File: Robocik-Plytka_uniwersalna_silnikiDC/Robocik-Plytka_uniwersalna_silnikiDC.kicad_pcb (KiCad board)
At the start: 2 copper layers, 60 x 66.8 mm, 67 parts, among them IC1 ACSL-6400-00TE, IC2 L6205D, J1 Conn_01x03, J2 Conn_01x02, J3 Conn_01x04, J4 Conn_01x02, J5 Conn_01x03, J6 Conn_01x02, Q1 BC847, Q2 BC847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

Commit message: Added connectors description on board.
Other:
- board text added: "CAN"
- board text added: "DC driver PCB v1"
- board text added: "Digital 5V"
- board text added: "Engines 16V"
- board text added: "Engines OUT"
- board text added: "UART"
- board text added: "programmer"
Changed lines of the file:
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@@
   (general
     (thickness 1.6)
-    (drawings 7)
+    (drawings 14)
     (tracks 496)
     (zones 0)
@@
     )
   )
+  (gr_text "DC driver PCB v1" (at 124.5 77.6 90) (layer F.SilkS)
+    (effects (font (size 1 1) (thickness 0.15)))
+  )
+  (gr_text "Engines OUT" (at 124 130.5 90) (layer F.SilkS)
+    (effects (font (size 1 1) (thickness 0.15)))
+  )
+  (gr_text "Engines 16V" (at 168.6 130.8 90) (layer F.SilkS)
+    (effects (font (size 1 1) (thickness 0.15)))
+  )
+  (gr_text UART (at 180.2 114.2 90) (layer F.SilkS)
+    (effects (font (size 1 1) (thickness 0.15)))
+  )
+  (gr_text CAN (at 180.2 103.3 90) (layer F.SilkS)
+    (effects (font (size 1 1) (thickness 0.15)))
+  )
+  (gr_text programmer (at 180 91.8 90) (layer F.SilkS)
+    (effects (font (size 1 1) (thickness 0.15)))
+  )
+  (gr_text "Digital 5V" (at 180.2 77.8 90) (layer F.SilkS)
+    (effects (font (size 1 1) (thickness 0.15)))
+  )
   (dimension 66.8 (width 0.15) (layer Dwgs.User)
     (gr_text "66,800 mm" (at 194.8 102.7 270) (layer Dwgs.User)
@@
   (gr_line (start 122.1 69.3) (end 122.1 135.5) (layer Edge.Cuts) (width 0.1))
   (gr_line (start 182.1 69.3) (end 122.1 69.3) (layer Edge.Cuts) (width 0.1))
-  (segment (start 143.93201 107.053222) (end 143.93201 109.16799) (width 0.25) (layer F.Cu) (net 76))
-  (segment (start 144 106.8) (end 144 106.985232) (width 0.25) (layer F.Cu) (net 76))
-  (segment (start 144 106.985232) (end 143.93201 107.053222) (width 0.25) (layer F.Cu) (net 76))
   (segment (start 145.176 95.051002) (end 145.866488 95.74149) (width 0.25) (layer F.Cu) (net 1))
   (segment (start 145.176 93.6045) (end 145.176 95.051002) (width 0.25) (layer F.Cu) (net 1))
@@
   (segment (start 141.609 81.568) (end 141.478 81.437) (width 0.5) (layer F.Cu) (net 75))
   (segment (start 143.942 81.568) (end 141.609 81.568) (width 0.5) (layer F.Cu) (net 75))
+  (segment (start 143.93201 107.053222) (end 143.93201 109.16799) (width 0.25) (layer F.Cu) (net 76))
+  (segment (start 144 106.8) (end 144 106.985232) (width 0.25) (layer F.Cu) (net 76))
+  (segment (start 144 106.985232) (end 143.93201 107.053222) (width 0.25) (layer F.Cu) (net 76))
   (via (at 143.256 116.84) (size 0.8) (drill 0.4) (layers F.Cu B.Cu) (net 76))
   (via (at 143.51 123.19) (size 0.8) (drill 0.4) (layers F.Cu B.Cu) (net 76))

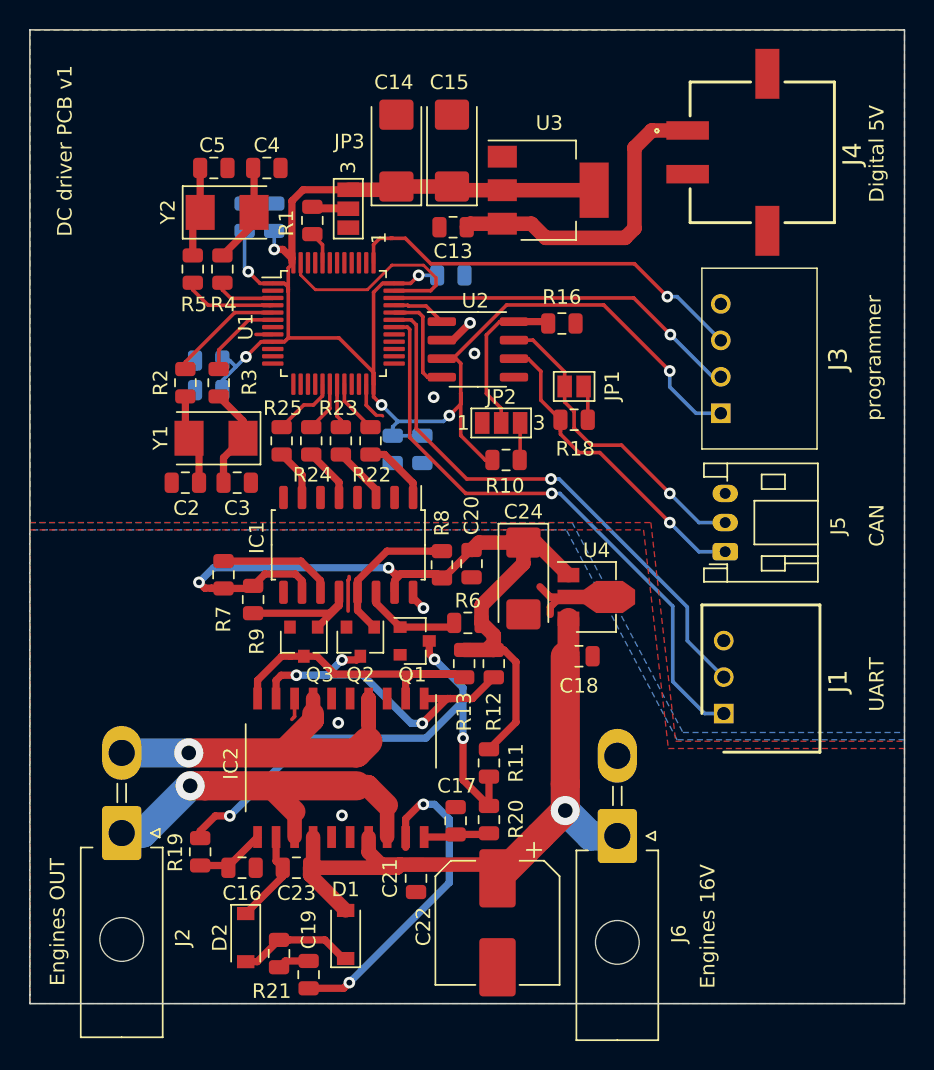
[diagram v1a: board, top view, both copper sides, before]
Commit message: Added missing 3D model for optocoupler. Moved all connector to the other side of the board. Reduced PCB size.
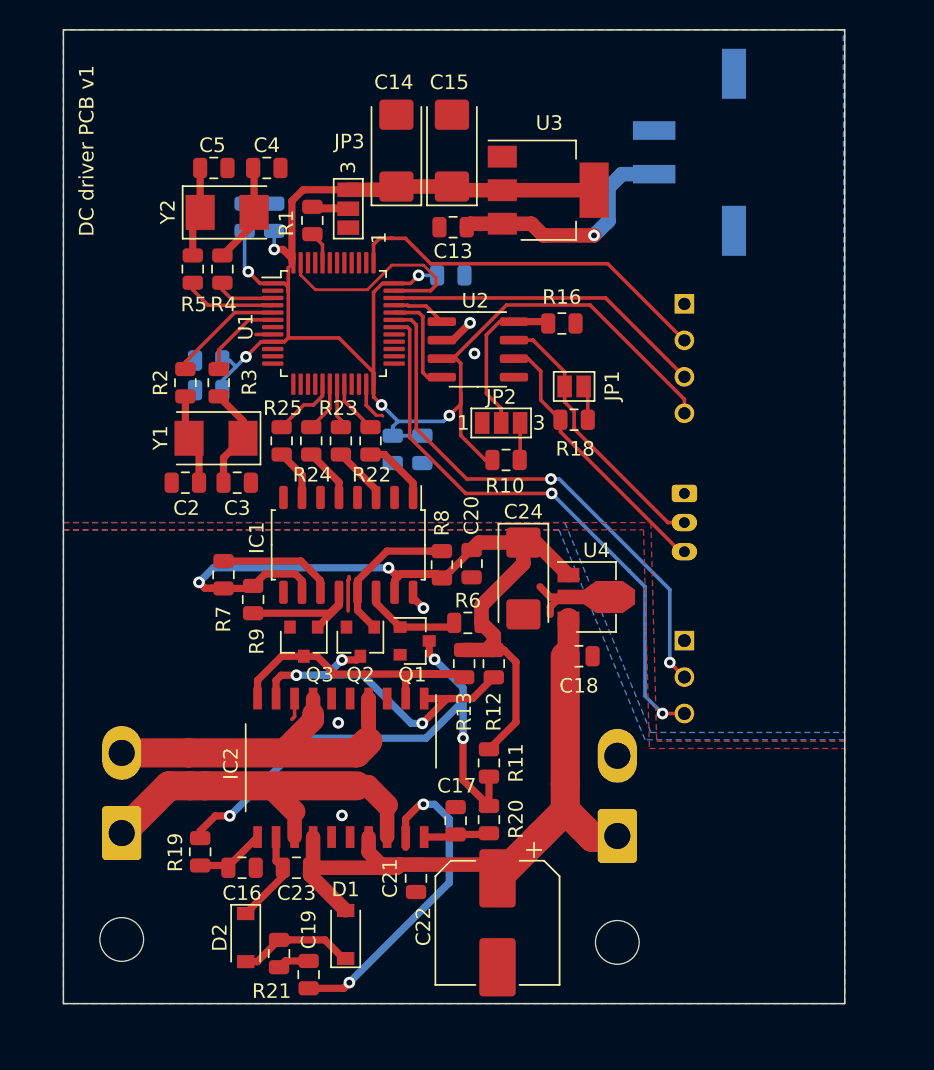
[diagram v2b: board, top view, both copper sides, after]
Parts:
- J1, J2, J3, J4, J5, J6: moved to B.Cu
- moved J3 7.91 mm to (167.0, 88.1), turned to 90 degrees
- moved J1 5.68 mm to (167.0, 111.2), turned to 90 degrees
- moved J5 4.88 mm to (167.0, 101.1), turned to 270 degrees
- moved J4 2.29 mm to (175.0, 77.7), turned to 270 degrees
- turned J2 to 0 degrees
- turned J6 to 0 degrees
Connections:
- J1 pad 1: USART_RX -> GNDD
- J1 pad 3: GNDD -> USART_RX
- J3 pad 1: 3.3VD -> GNDD
- J3 pad 2: JTMS_SWDIO -> JTCK_SWCLK
- J3 pad 3: JTCK_SWCLK -> JTMS_SWDIO
- J3 pad 4: GNDD -> 3.3VD
- J5 pad 1: CAN_L -> GNDD
- J5 pad 3: GNDD -> CAN_L
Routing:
- net VddD: track 21.9 -> 16.7 mm, vias 0 -> 1
- net CAN_L: track 22.9 -> 18.8 mm, vias 1 -> 0
- net JTMS_SWDIO: track 25.0 -> 22.2 mm, vias 1 -> 0
- net CAN_H: track 21.6 -> 18.8 mm, vias 1 -> 0
- net JTCK_SWCLK: track 28.5 -> 25.8 mm, vias 1 -> 0
- net 3.3VD: track 118.8 -> 116.2 mm, vias 7 -> 6
- net USART_RX: track 41.0 -> 39.6 mm, vias 1 -> 2
- net USART_TX: track 38.3 -> 37.2 mm, vias 1 -> 2
- net VddPWR: track 47.1 -> 47.3 mm, vias 1 -> 0
- net GNDD: vias 3 -> 2
- net ENG2: vias 1 -> 0
- net ENG1: vias 1 -> 0
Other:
- board size 60 x 66.8 mm -> 53.6 x 66.8 mm

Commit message: Further reduce of PCB size - moved description of every connector away from the border of PCB.
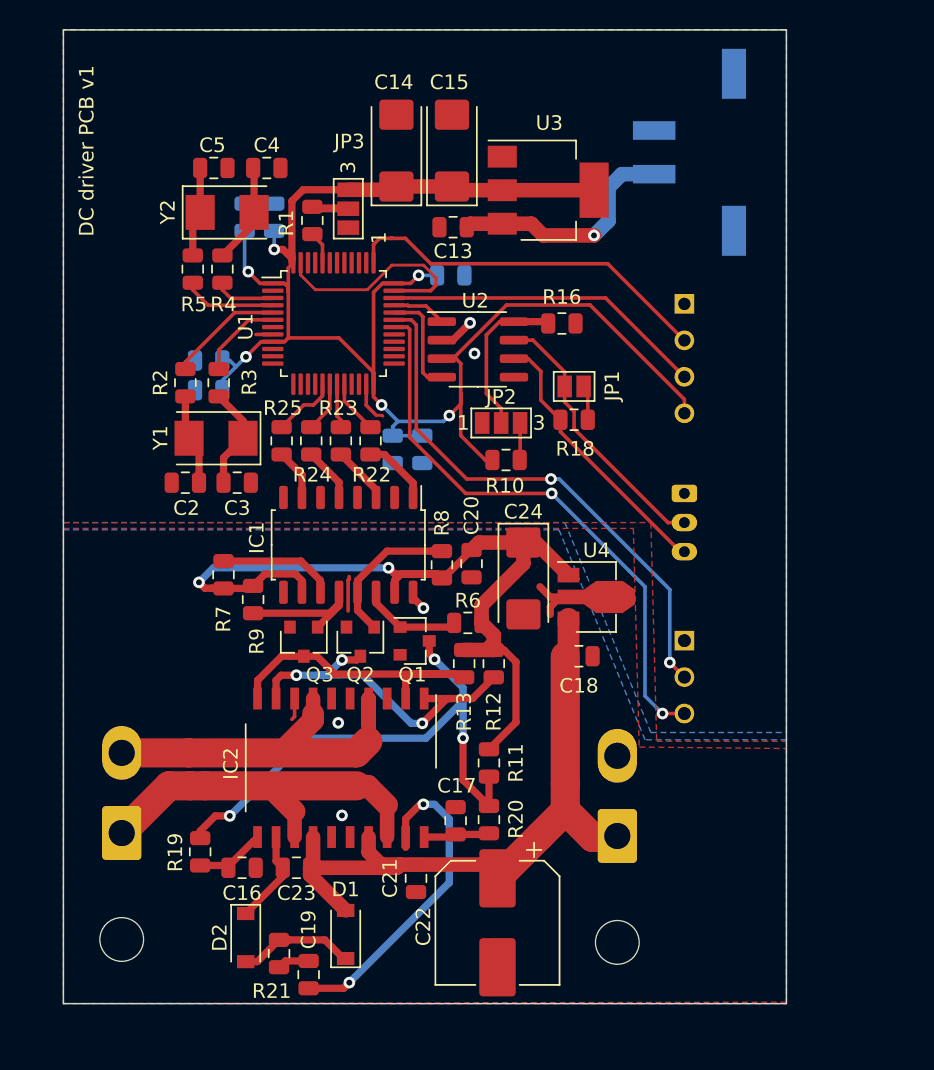
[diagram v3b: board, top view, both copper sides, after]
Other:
- board size 53.6 x 66.8 mm -> 49.6 x 66.8 mm
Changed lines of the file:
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@@
     (effects (font (size 1 1) (thickness 0.15)) (justify mirror))
   )
-  (gr_text UART (at 175 114.2 90) (layer B.SilkS)
+  (gr_text UART (at 162 113.402 90) (layer B.SilkS)
     (effects (font (size 1 1) (thickness 0.15)) (justify mirror))
   )
-  (gr_text CAN (at 175 103.3 90) (layer B.SilkS)
+  (gr_text CAN (at 162 102.87 90) (layer B.SilkS)
     (effects (font (size 1 1) (thickness 0.15)) (justify mirror))
   )
-  (gr_text programmer (at 175 91.8 90) (layer B.SilkS)
+  (gr_text programmer (at 162 91.8 90) (layer B.SilkS)
     (effects (font (size 1 1) (thickness 0.15)) (justify mirror))
   )
-  (gr_text "Digital 5V" (at 177 77.8 90) (layer B.SilkS)
+  (gr_text "Digital 5V" (at 160 77.8 90) (layer B.SilkS)
     (effects (font (size 1 1) (thickness 0.15)) (justify mirror))
   )
   (dimension 66.8 (width 0.15) (layer Dwgs.User)
-    (gr_text "66,800 mm" (at 190.7 102.7 270) (layer Dwgs.User)
+    (gr_text "66,800 mm" (at 186.7 102.7 270) (layer Dwgs.User)
       (effects (font (size 1 1) (thickness 0.15)))
     )
-    (feature1 (pts (xy 178 136.1) (xy 189.986421 136.1)))
-    (feature2 (pts (xy 178 69.3) (xy 189.986421 69.3)))
-    (crossbar (pts (xy 189.4 69.3) (xy 189.4 136.1)))
-    (arrow1a (pts (xy 189.4 136.1) (xy 188.813579 134.973496)))
-    (arrow1b (pts (xy 189.4 136.1) (xy 189.986421 134.973496)))
-    (arrow2a (pts (xy 189.4 69.3) (xy 188.813579 70.426504)))
-    (arrow2b (pts (xy 189.4 69.3) (xy 189.986421 70.426504)))
-  )
-  (dimension 53.6 (width 0.15) (layer Dwgs.User)
-    (gr_text "53,600 mm" (at 151.2 61.7) (layer Dwgs.User)
+    (feature1 (pts (xy 174 136.1) (xy 185.986421 136.1)))
+    (feature2 (pts (xy 174 69.3) (xy 185.986421 69.3)))
+    (crossbar (pts (xy 185.4 69.3) (xy 185.4 136.1)))
+    (arrow1a (pts (xy 185.4 136.1) (xy 184.813579 134.973496)))
+    (arrow1b (pts (xy 185.4 136.1) (xy 185.986421 134.973496)))
+    (arrow2a (pts (xy 185.4 69.3) (xy 184.813579 70.426504)))
+    (arrow2b (pts (xy 185.4 69.3) (xy 185.986421 70.426504)))
+  )
+  (dimension 49.6 (width 0.15) (layer Dwgs.User)
+    (gr_text "49,600 mm" (at 149.2 61.7) (layer Dwgs.User)
       (effects (font (size 1 1) (thickness 0.15)))
     )
-    (feature1 (pts (xy 178 69.3) (xy 178 62.413579)))
+    (feature1 (pts (xy 174 69.3) (xy 174 62.413579)))
     (feature2 (pts (xy 124.4 69.3) (xy 124.4 62.413579)))
-    (crossbar (pts (xy 124.4 63) (xy 178 63)))
-    (arrow1a (pts (xy 178 63) (xy 176.873496 63.586421)))
-    (arrow1b (pts (xy 178 63) (xy 176.873496 62.413579)))
+    (crossbar (pts (xy 124.4 63) (xy 174 63)))
+    (arrow1a (pts (xy 174 63) (xy 172.873496 63.586421)))
+    (arrow1b (pts (xy 174 63) (xy 172.873496 62.413579)))
     (arrow2a (pts (xy 124.4 63) (xy 125.526504 63.586421)))
     (arrow2b (pts (xy 124.4 63) (xy 125.526504 62.413579)))
   )
-  (gr_line (start 178 136.1) (end 178 69.3) (layer Edge.Cuts) (width 0.1))
-  (gr_line (start 124.4 136.1) (end 178 136.1) (layer Edge.Cuts) (width 0.1))
+  (gr_line (start 174 136.1) (end 174 69.3) (layer Edge.Cuts) (width 0.1))
+  (gr_line (start 124.4 136.1) (end 174 136.1) (layer Edge.Cuts) (width 0.1))
   (gr_line (start 124.4 69.3) (end 124.4 136.1) (layer Edge.Cuts) (width 0.1))
-  (gr_line (start 178 69.3) (end 124.4 69.3) (layer Edge.Cuts) (width 0.1))
+  (gr_line (start 174 69.3) (end 124.4 69.3) (layer Edge.Cuts) (width 0.1))
   (segment (start 145.176 95.051002) (end 145.866488 95.74149) (width 0.25) (layer F.Cu) (net 1))
   (segment (start 145.176 93.6045) (end 145.176 95.051002) (width 0.25) (layer F.Cu) (net 1))
@@
     (polygon
       (pts
-        (xy 124.4 69.3) (xy 124.4 103.1) (xy 164.7 103.1) (xy 165.1 118.1) (xy 178 118.1)
-        (xy 178 69.3)
+        (xy 124.4 69.3) (xy 124.4 103.1) (xy 164.7 103.1) (xy 165.1 118.1) (xy 174 118.1)
+        (xy 174 69.3)
       )
     )
@@
     (polygon
       (pts
-        (xy 124.4 103.6) (xy 164.2 103.6) (xy 164.6 118.6) (xy 178 118.6) (xy 178 136.1)
+        (xy 124.4 103.5) (xy 163.5 103.5) (xy 163.9 118.5) (xy 174 118.6) (xy 174 136)
         (xy 124.4 136.1)
       )
@@
     (polygon
       (pts
-        (xy 124.4 69.3) (xy 124.4 103.1) (xy 158.8 103.1) (xy 164.7 117.5) (xy 178 117.5)
-        (xy 177.9 69.3)
+        (xy 124.4 69.3) (xy 124.4 103.1) (xy 158.8 103.1) (xy 164.7 117.5) (xy 174 117.5)
+        (xy 174 69.3)
       )
     )
@@
     (polygon
       (pts
-        (xy 124.4 103.6) (xy 124.4 136.1) (xy 178 136.1) (xy 178 118) (xy 164.3 118)
+        (xy 124.4 103.6) (xy 124.4 136.1) (xy 174 136.1) (xy 174 118) (xy 164.3 118)
         (xy 158.4 103.6)
       )
